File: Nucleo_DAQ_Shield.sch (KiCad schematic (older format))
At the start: 30 parts, among them J1 CONN_01X06, J2 CONN_01X06, J3 CONN_01X02, J4 CONN_01X02, J5 CONN_01X02, J6 CONN_COAXIAL, U1 4050, U10 ST_Nucleo144_F746ZG_CN10, U2 TL072, U3 7805, U4 TLV70233DBV, U5 DRV8881, U7 ST_Nucleo144_F746ZG_CN7, U8 ST_Nucleo144_F746ZG_CN8, U9 ST__Nucleo144_F746ZG_CN9

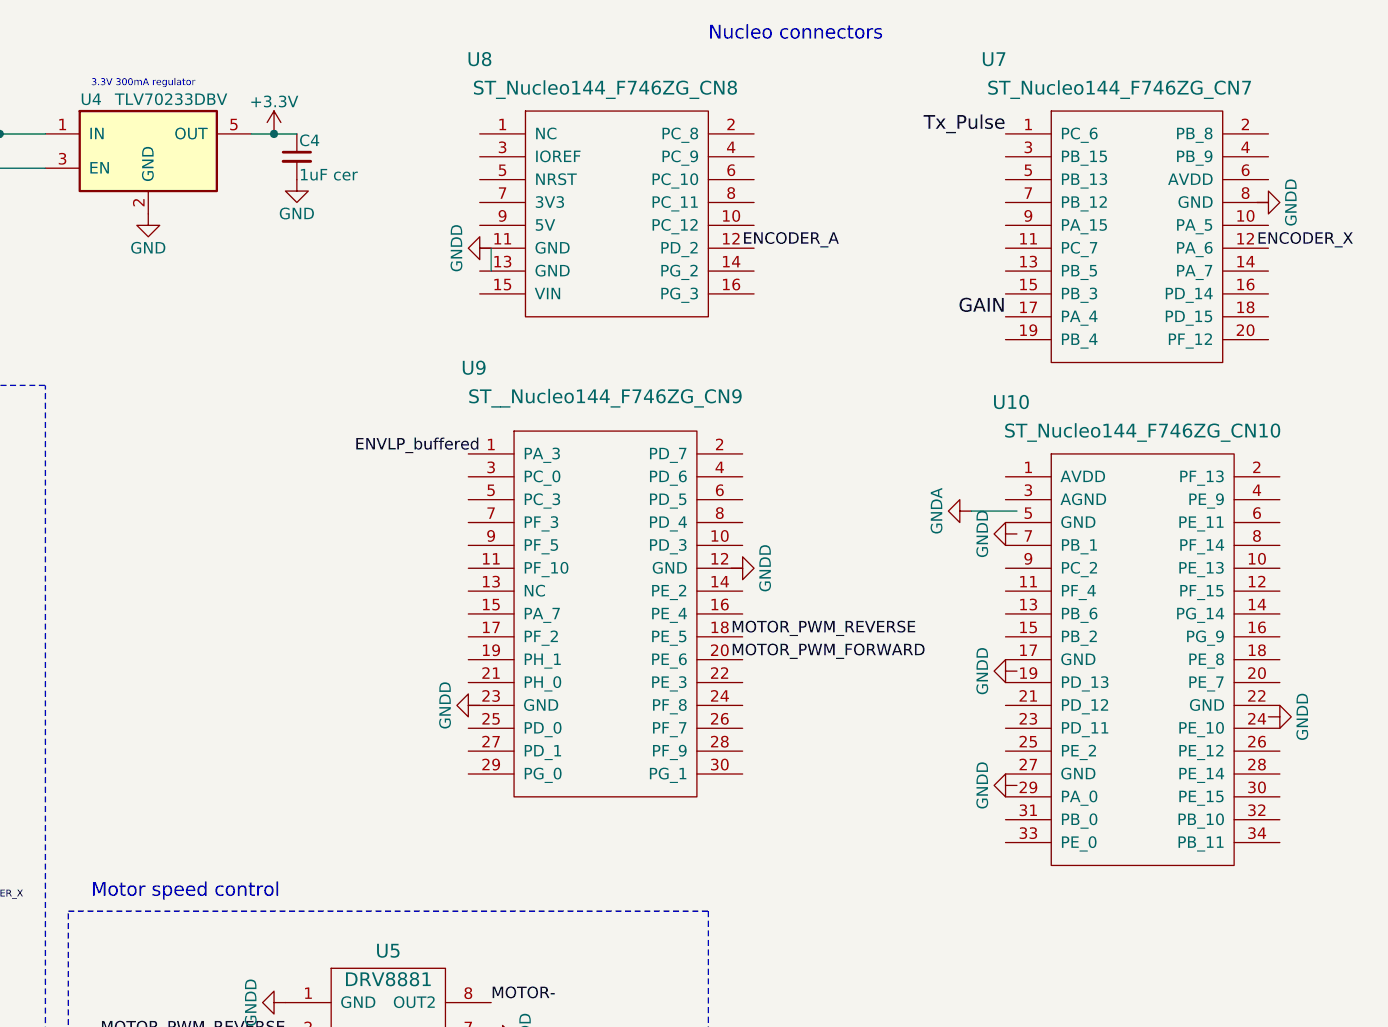
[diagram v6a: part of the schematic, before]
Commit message: Updated Nucleo connectors in schematic
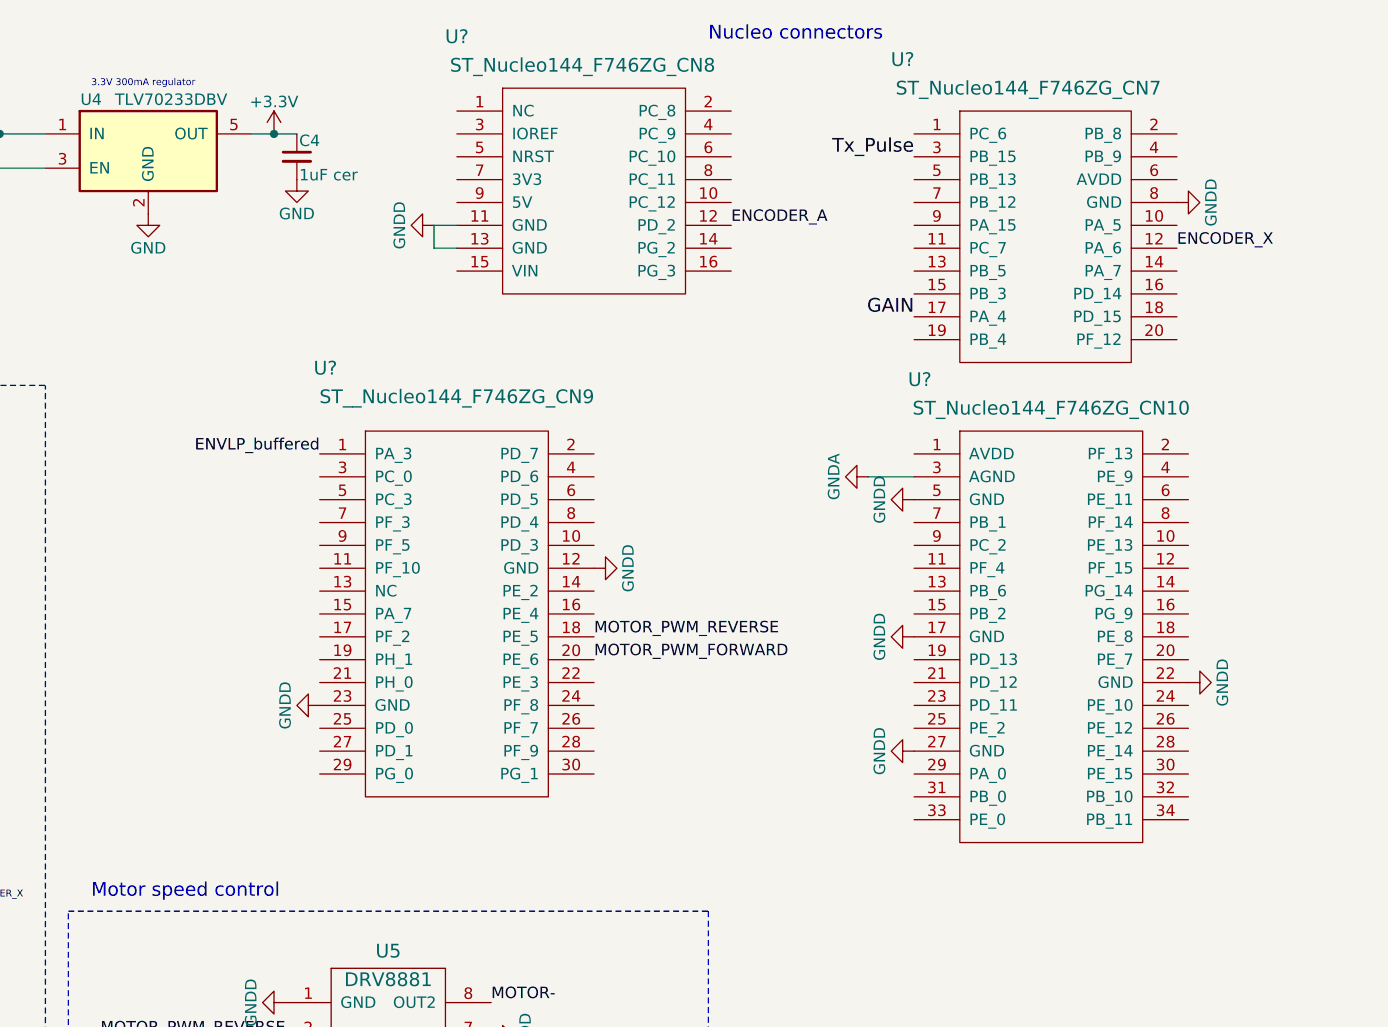
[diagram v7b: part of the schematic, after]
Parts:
- removed U10: ST_Nucleo144_F746ZG_CN10, symbol ST_Nucleo144_F746ZG_CN10
- removed U7: ST_Nucleo144_F746ZG_CN7, symbol ST_Nucleo144_F746ZG_CN7
- removed U8: ST_Nucleo144_F746ZG_CN8, symbol ST_Nucleo144_F746ZG_CN8
- removed U9: ST__Nucleo144_F746ZG_CN9, symbol ST__Nucleo144_F746ZG_CN9
- added U?: ST_Nucleo144_F746ZG_CN8, symbol ST_Nucleo144_F746ZG_CN8
- added U?: ST_Nucleo144_F746ZG_CN7, symbol ST_Nucleo144_F746ZG_CN7
- added U?: ST__Nucleo144_F746ZG_CN9, symbol ST__Nucleo144_F746ZG_CN9
- added U?: ST_Nucleo144_F746ZG_CN10, symbol ST_Nucleo144_F746ZG_CN10
- C1: footprint (none) -> Capacitors_Tantalum_SMD:CP_Tantalum_Case-A_EIA-3216-18_Hand
- C2, C3: footprint (none) -> Capacitors_SMD:C_0603
- U5: footprint (none) -> Housings_SOIC:SOIC-8_3.9x4.9mm_Pitch1.27mm
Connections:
- wire segments 47 -> 49

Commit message: --amend
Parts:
- gave numbers to parts that had none: 4
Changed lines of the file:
@@
 	2500 7000 2800 7000
 $Comp
-L ST_Nucleo144_F746ZG_CN8 U?
+L ST_Nucleo144_F746ZG_CN8 U8
 U 1 1 59645D15
 P 7900 1250
-F 0 "U?" H 7300 1925 60  0000 C CNN
+F 0 "U8" H 7300 1925 60  0000 C CNN
 F 1 "ST_Nucleo144_F746ZG_CN8" H 7850 1800 60  0000 C CNN
 F 2 "" H 7800 450 60  0001 C CNN
@@
 	7200 1400 7300 1400
 $Comp
-L ST_Nucleo144_F746ZG_CN7 U?
+L ST_Nucleo144_F746ZG_CN7 U7
 U 1 1 59646625
 P 9850 1350
-F 0 "U?" H 9250 2025 60  0000 C CNN
+F 0 "U7" H 9250 2025 60  0000 C CNN
 F 1 "ST_Nucleo144_F746ZG_CN7" H 9800 1900 60  0000 C CNN
 F 2 "" H 9750 550 60  0001 C CNN
@@
 $EndComp
 $Comp
-L ST__Nucleo144_F746ZG_CN9 U?
+L ST__Nucleo144_F746ZG_CN9 U9
 U 1 1 59646EE4
 P 7300 3100
-F 0 "U?" H 6725 4175 60  0000 C CNN
+F 0 "U9" H 6725 4175 60  0000 C CNN
 F 1 "ST__Nucleo144_F746ZG_CN9" H 7300 4050 60  0000 C CNN
 F 2 "" H 7200 3950 60  0001 C CNN
@@
 $EndComp
 $Comp
-L ST_Nucleo144_F746ZG_CN10 U?
+L ST_Nucleo144_F746ZG_CN10 U10
 U 1 1 5964764D
 P 9900 3150
-F 0 "U?" H 9325 4225 60  0000 C CNN
+F 0 "U10" H 9325 4225 60  0000 C CNN
 F 1 "ST_Nucleo144_F746ZG_CN10" H 9900 4100 60  0000 C CNN
 F 2 "" H 9800 4000 60  0001 C CNN
